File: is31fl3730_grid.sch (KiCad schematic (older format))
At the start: 8 parts

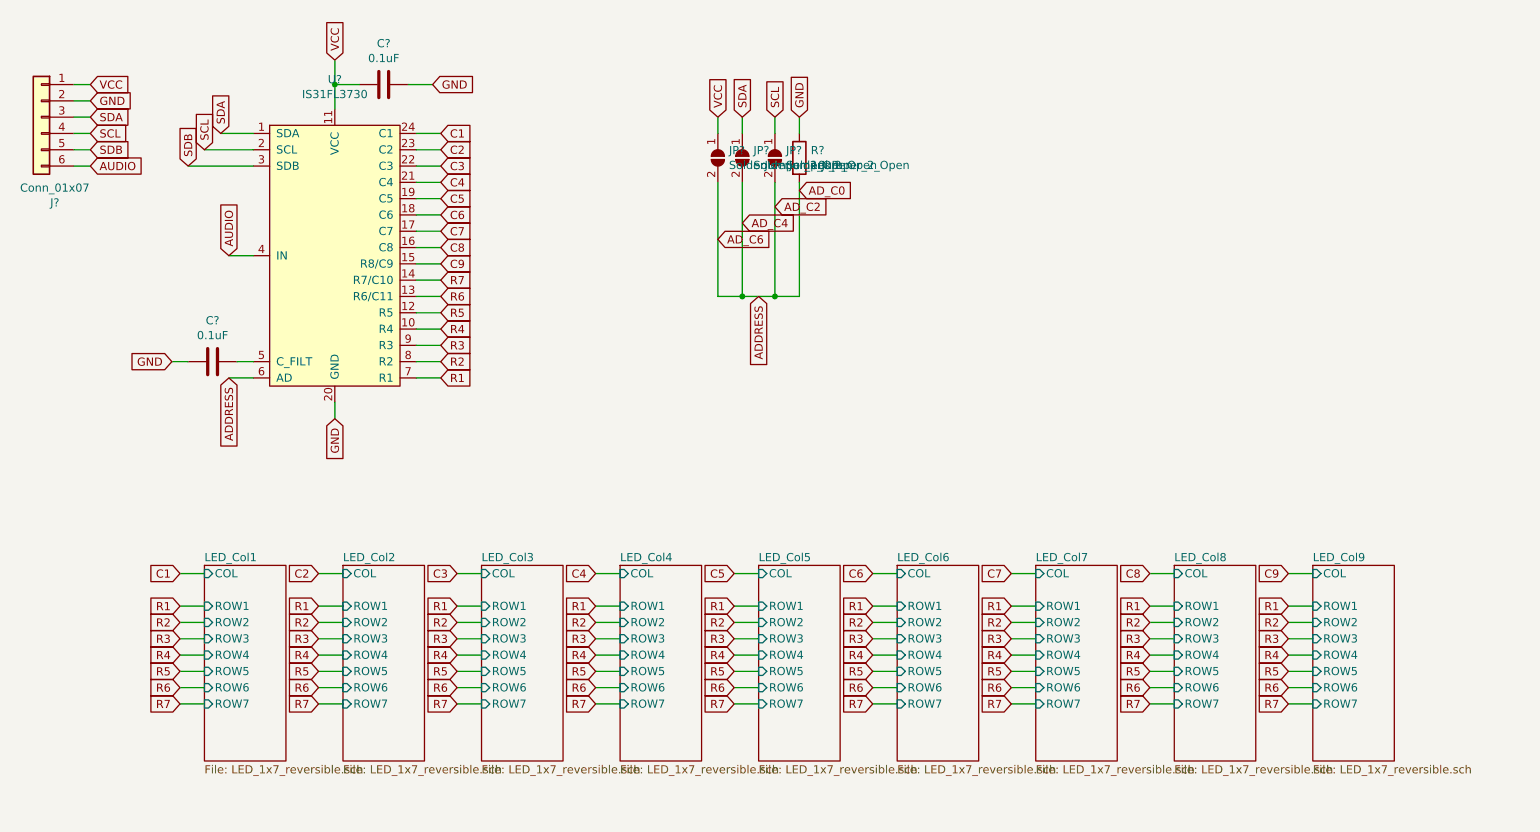
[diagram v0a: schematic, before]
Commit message: Placed 14x9 grid
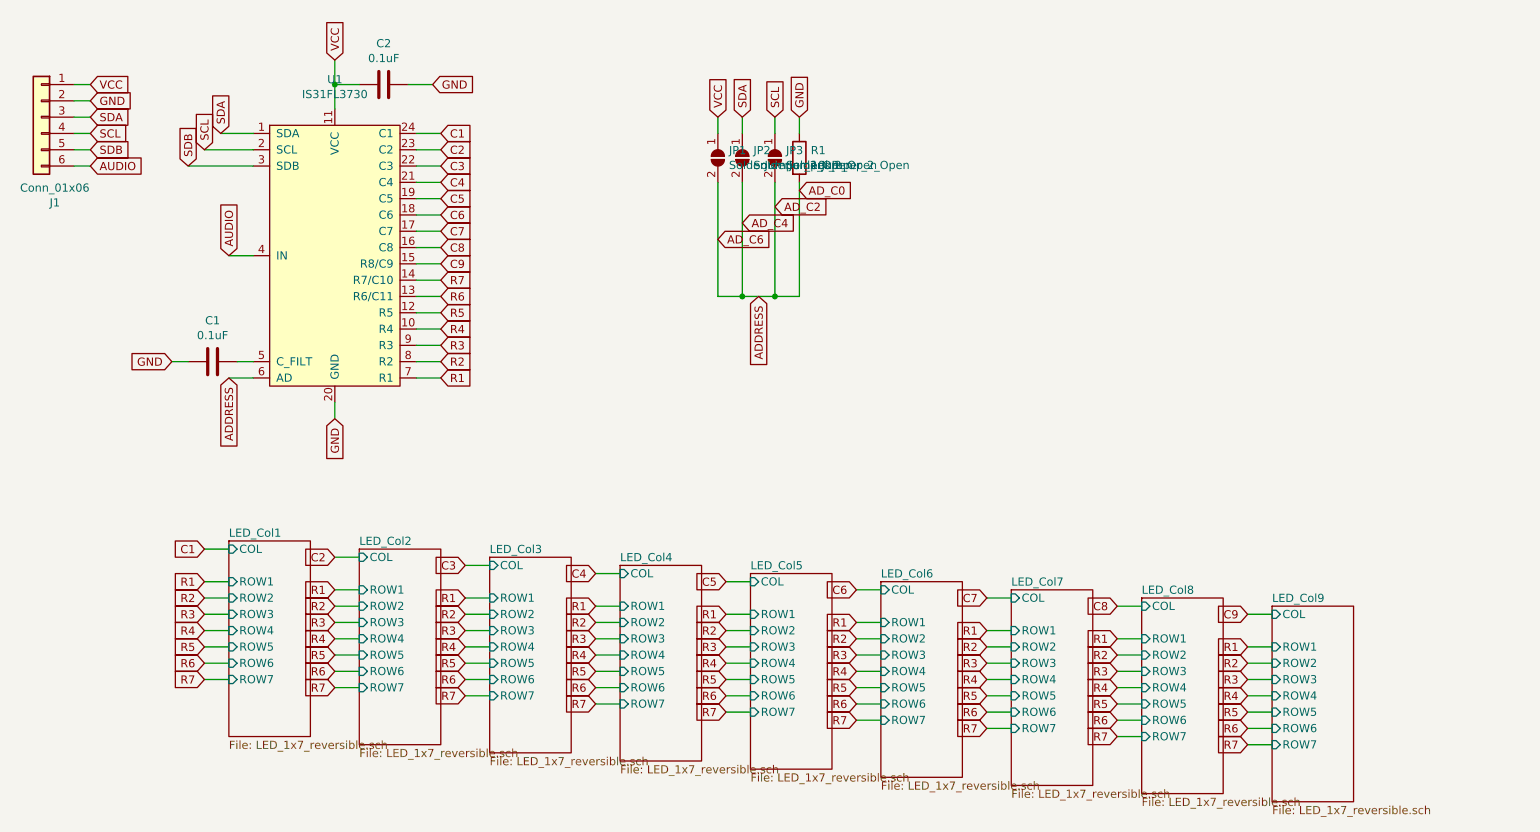
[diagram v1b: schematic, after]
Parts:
- C1, C2: renamed from C?; footprint (none) -> Capacitor_SMD:C_0603_1608Metric
- J1: renamed from J?; value Conn_01x07 -> Conn_01x06; footprint (none) -> Connector_PinHeader_2.54mm:PinHeader_1x06_P2.54mm_Vertical
- JP1, JP2, JP3: renamed from JP?; footprint (none) -> Jumper:SolderJumper-2_P1.3mm_Open_TrianglePad1.0x1.5mm
- R1: renamed from R?; footprint (none) -> Resistor_SMD:R_0805_2012Metric
- gave numbers to parts that had none: 1

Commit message: Fix matrix
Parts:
- added R2: 10kR, Resistor_SMD:R_0805_2012Metric, symbol Device:R
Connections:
- net SDB: now also R2.1
- net VCC: now also R2.2
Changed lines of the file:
@@
 Wire Wire Line
 	2950 4050 2800 4050
+Text GLabel 6650 1150 1    50   Input ~ 0
+SDB
+Text GLabel 6650 1650 3    50   Input ~ 0
+VCC
+$Comp
+L Device:R R2
+U 1 1 5EC28526
+P 6650 1400
+F 0 "R2" H 6720 1446 50  0000 L CNN
+F 1 "10kR" H 6720 1355 50  0000 L CNN
+F 2 "Resistor_SMD:R_0805_2012Metric" V 6580 1400 50  0001 C CNN
+F 3 "~" H 6650 1400 50  0001 C CNN
+	1    6650 1400
+	1    0    0    -1
+$EndComp
+Wire Wire Line
+	6650 1150 6650 1250
+Wire Wire Line
+	6650 1550 6650 1650
 $EndSCHEMATC
